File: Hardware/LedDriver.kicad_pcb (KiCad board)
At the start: 2 copper layers, 38 x 17 mm, 10 parts, among them J1 Led connector, U1 AP3019A

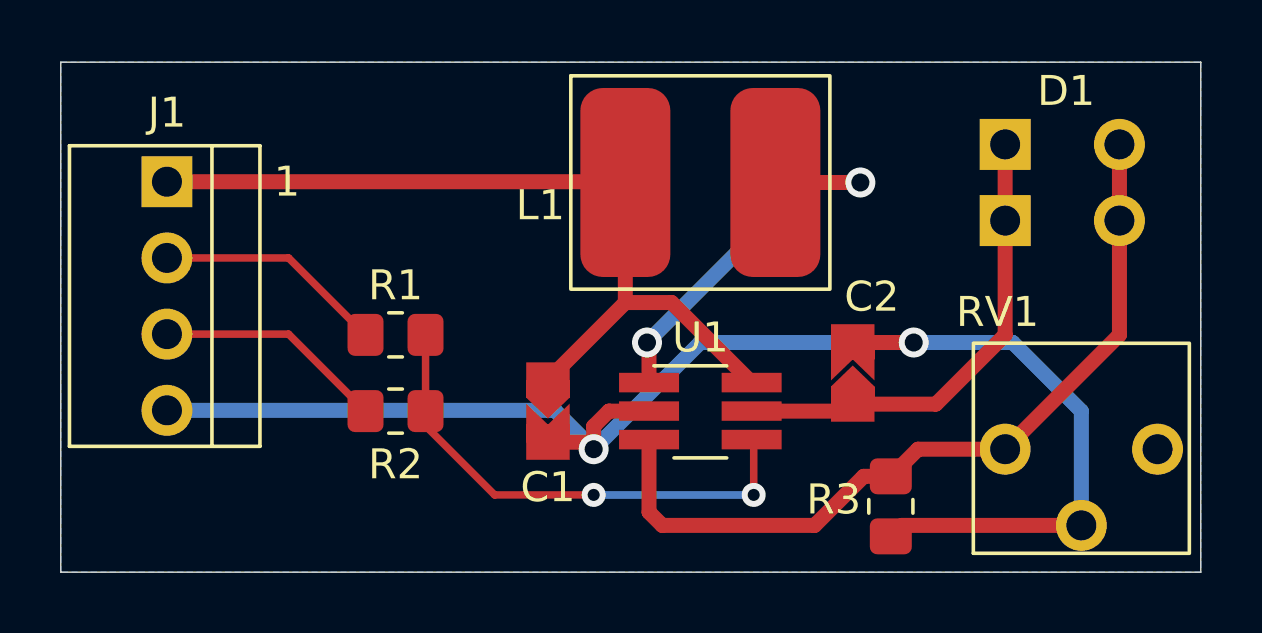
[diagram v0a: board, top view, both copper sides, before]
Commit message: ledDriver: added ground plane on top
+ added vias
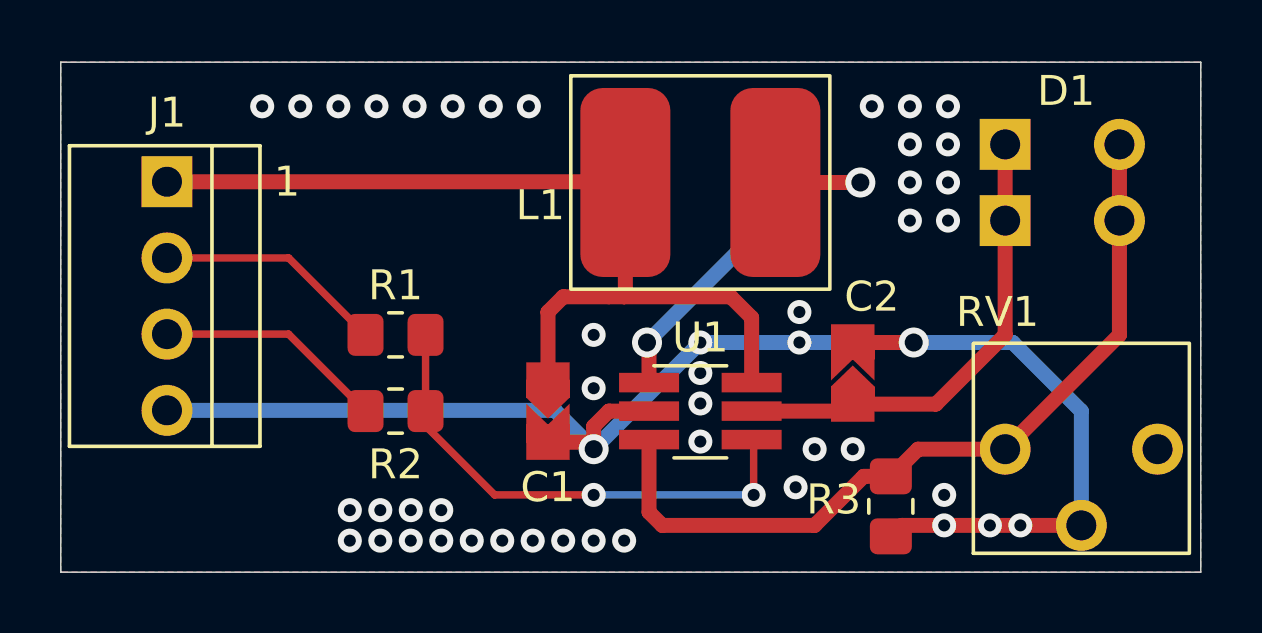
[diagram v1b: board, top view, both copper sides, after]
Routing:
- net VCC: track 28.3 -> 30.8 mm
- net GND: vias 2 -> 48
- added copper zone on F.Cu, net GND
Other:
- board text added: "Led driver Esseiva Nicolas 2023.05.07 - R01"
- board text removed: "Led driver Esseiva Nicolas 2023.04.07 - R00"
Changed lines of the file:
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@@
   )
   (gr_rect (start 126 76) (end 164 93) (layer "Edge.Cuts") (width 0.05) (fill none))
-  (gr_text "Led driver\nEsseiva Nicolas\n2023.04.07 - R00" (at 145 81.5) (layer "B.SilkS")
+  (gr_text "Led driver\nEsseiva Nicolas\n2023.05.07 - R01" (at 145 81.5) (layer "B.SilkS")
     (effects (font (size 1.5 1.5) (thickness 0.3)))
   )
@@
   (segment (start 129.54 79.985) (end 144.795 79.985) (width 0.5) (layer "F.Cu") (net 1))
   (segment (start 144.795 79.985) (end 144.82 80.01) (width 0.5) (layer "F.Cu") (net 1))
-  (segment (start 149.03 86.68) (end 146.3625 84.0125) (width 0.5) (layer "F.Cu") (net 1))
-  (segment (start 144.82 80.01) (end 144.82 84.0125) (width 0.5) (layer "F.Cu") (net 1))
-  (segment (start 144.82 84.0125) (end 142.24 86.5925) (width 0.5) (layer "F.Cu") (net 1))
-  (segment (start 146.3625 84.0125) (end 144.82 84.0125) (width 0.5) (layer "F.Cu") (net 1))
-  (segment (start 154.035 91.44) (end 160.02 91.44) (width 0.5) (layer "F.Cu") (net 2))
+  (segment (start 142.748 83.82) (end 142.24 84.328) (width 0.5) (layer "F.Cu") (net 1))
+  (segment (start 149.03 86.68) (end 149.03 84.514) (width 0.5) (layer "F.Cu") (net 1))
+  (segment (start 144.272 83.82) (end 142.748 83.82) (width 0.5) (layer "F.Cu") (net 1))
+  (segment (start 149.03 84.514) (end 148.336 83.82) (width 0.5) (layer "F.Cu") (net 1))
+  (segment (start 142.24 84.328) (end 142.24 86.5925) (width 0.5) (layer "F.Cu") (net 1))
+  (segment (start 148.336 83.82) (end 144.78 83.82) (width 0.5) (layer "F.Cu") (net 1))
+  (segment (start 144.82 80.01) (end 144.82 83.78) (width 0.5) (layer "F.Cu") (net 1))
+  (segment (start 144.82 83.78) (end 144.78 83.82) (width 0.5) (layer "F.Cu") (net 1))
+  (segment (start 144.78 83.82) (end 144.272 83.82) (width 0.5) (layer "F.Cu") (net 1))
+  (segment (start 157.988 91.44) (end 160.02 91.44) (width 0.5) (layer "F.Cu") (net 2))
+  (segment (start 154.035 91.44) (end 155.448 91.44) (width 0.5) (layer "F.Cu") (net 2))
+  (segment (start 156.972 91.44) (end 157.988 91.44) (width 0.5) (layer "F.Cu") (net 2))
   (segment (start 152.4215 85.344) (end 152.4 85.3225) (width 0.5) (layer "F.Cu") (net 2))
   (segment (start 145.61 87.63) (end 144.272 87.63) (width 0.5) (layer "F.Cu") (net 2))
   (segment (start 154.432 85.344) (end 152.4215 85.344) (width 0.5) (layer "F.Cu") (net 2))
   (segment (start 142.24 88.6675) (end 143.5315 88.6675) (width 0.5) (layer "F.Cu") (net 2))
+  (segment (start 155.448 91.44) (end 156.972 91.44) (width 0.5) (layer "F.Cu") (net 2))
   (segment (start 143.5315 88.6675) (end 143.764 88.9) (width 0.5) (layer "F.Cu") (net 2))
   (segment (start 153.67 91.805) (end 154.035 91.44) (width 0.5) (layer "F.Cu") (net 2))
   (segment (start 144.272 87.63) (end 143.764 88.138) (width 0.5) (layer "F.Cu") (net 2))
   (segment (start 143.764 88.138) (end 143.764 88.9) (width 0.5) (layer "F.Cu") (net 2))
+  (via (at 136.525 77.47) (size 0.8) (drill 0.4) (layers "F.Cu" "B.Cu") (free) (net 2))
+  (via (at 141.732 91.948) (size 0.8) (drill 0.4) (layers "F.Cu" "B.Cu") (free) (net 2))
+  (via (at 156.972 91.44) (size 0.8) (drill 0.4) (layers "F.Cu" "B.Cu") (net 2))
+  (via (at 139.065 77.47) (size 0.8) (drill 0.4) (layers "F.Cu" "B.Cu") (free) (net 2))
+  (via (at 154.305 77.47) (size 0.8) (drill 0.4) (layers "F.Cu" "B.Cu") (free) (net 2))
+  (via (at 143.764 91.948) (size 0.8) (drill 0.4) (layers "F.Cu" "B.Cu") (free) (net 2))
+  (via (at 157.988 91.44) (size 0.8) (drill 0.4) (layers "F.Cu" "B.Cu") (net 2))
+  (via (at 133.985 77.47) (size 0.8) (drill 0.4) (layers "F.Cu" "B.Cu") (free) (net 2))
+  (via (at 139.7 91.948) (size 0.8) (drill 0.4) (layers "F.Cu" "B.Cu") (free) (net 2))
+  (via (at 140.335 77.47) (size 0.8) (drill 0.4) (layers "F.Cu" "B.Cu") (free) (net 2))
+  (via (at 154.305 78.74) (size 0.8) (drill 0.4) (layers "F.Cu" "B.Cu") (free) (net 2))
+  (via (at 138.684 91.948) (size 0.8) (drill 0.4) (layers "F.Cu" "B.Cu") (free) (net 2))
+  (via (at 137.795 77.47) (size 0.8) (drill 0.4) (layers "F.Cu" "B.Cu") (free) (net 2))
+  (via (at 152.4 88.9) (size 0.8) (drill 0.4) (layers "F.Cu" "B.Cu") (free) (net 2))
+  (via (at 137.668 90.932) (size 0.8) (drill 0.4) (layers "F.Cu" "B.Cu") (free) (net 2))
+  (via (at 154.305 81.28) (size 0.8) (drill 0.4) (layers "F.Cu" "B.Cu") (free) (net 2))
   (via (at 143.764 88.9) (size 1) (drill 0.6) (layers "F.Cu" "B.Cu") (net 2))
+  (via (at 137.668 91.948) (size 0.8) (drill 0.4) (layers "F.Cu" "B.Cu") (free) (net 2))
+  (via (at 135.636 91.948) (size 0.8) (drill 0.4) (layers "F.Cu" "B.Cu") (free) (net 2))
+  (via (at 144.78 91.948) (size 0.8) (drill 0.4) (layers "F.Cu" "B.Cu") (free) (net 2))
+  (via (at 135.636 90.932) (size 0.8) (drill 0.4) (layers "F.Cu" "B.Cu") (free) (net 2))
+  (via (at 147.32 88.646) (size 0.8) (drill 0.4) (layers "F.Cu" "B.Cu") (free) (net 2))
+  (via (at 138.684 90.932) (size 0.8) (drill 0.4) (layers "F.Cu" "B.Cu") (free) (net 2))
+  (via (at 155.575 81.28) (size 0.8) (drill 0.4) (layers "F.Cu" "B.Cu") (free) (net 2))
+  (via (at 136.652 90.932) (size 0.8) (drill 0.4) (layers "F.Cu" "B.Cu") (free) (net 2))
+  (via (at 150.622 84.328) (size 0.8) (drill 0.4) (layers "F.Cu" "B.Cu") (free) (net 2))
+  (via (at 155.575 80.01) (size 0.8) (drill 0.4) (layers "F.Cu" "B.Cu") (free) (net 2))
+  (via (at 154.305 80.01) (size 0.8) (drill 0.4) (layers "F.Cu" "B.Cu") (free) (net 2))
+  (via (at 141.605 77.47) (size 0.8) (drill 0.4) (layers "F.Cu" "B.Cu") (free) (net 2))
+  (via (at 143.764 85.09) (size 0.8) (drill 0.4) (layers "F.Cu" "B.Cu") (free) (net 2))
+  (via (at 150.622 85.344) (size 0.8) (drill 0.4) (layers "F.Cu" "B.Cu") (net 2))
+  (via (at 150.495 90.17) (size 0.8) (drill 0.4) (layers "F.Cu" "B.Cu") (free) (net 2))
+  (via (at 155.448 91.44) (size 0.8) (drill 0.4) (layers "F.Cu" "B.Cu") (net 2))
+  (via (at 153.035 77.47) (size 0.8) (drill 0.4) (layers "F.Cu" "B.Cu") (free) (net 2))
+  (via (at 140.716 91.948) (size 0.8) (drill 0.4) (layers "F.Cu" "B.Cu") (free) (net 2))
+  (via (at 136.652 91.948) (size 0.8) (drill 0.4) (layers "F.Cu" "B.Cu") (free) (net 2))
+  (via (at 142.748 91.948) (size 0.8) (drill 0.4) (layers "F.Cu" "B.Cu") (free) (net 2))
+  (via (at 155.448 90.424) (size 0.8) (drill 0.4) (layers "F.Cu" "B.Cu") (free) (net 2))
+  (via (at 132.715 77.47) (size 0.8) (drill 0.4) (layers "F.Cu" "B.Cu") (free) (net 2))
+  (via (at 155.575 78.74) (size 0.8) (drill 0.4) (layers "F.Cu" "B.Cu") (free) (net 2))
+  (via (at 147.32 85.344) (size 0.8) (drill 0.4) (layers "F.Cu" "B.Cu") (net 2))
+  (via (at 155.575 77.47) (size 0.8) (drill 0.4) (layers "F.Cu" "B.Cu") (free) (net 2))
+  (via (at 147.32 86.36) (size 0.8) (drill 0.4) (layers "F.Cu" "B.Cu") (free) (net 2))
+  (via (at 135.255 77.47) (size 0.8) (drill 0.4) (layers "F.Cu" "B.Cu") (free) (net 2))
+  (via (at 151.13 88.9) (size 0.8) (drill 0.4) (layers "F.Cu" "B.Cu") (free) (net 2))
   (via (at 154.432 85.344) (size 1) (drill 0.6) (layers "F.Cu" "B.Cu") (net 2))
-  (segment (start 147.32 85.344) (end 154.432 85.344) (width 0.5) (layer "B.Cu") (net 2))
+  (via (at 143.764 86.868) (size 0.8) (drill 0.4) (layers "F.Cu" "B.Cu") (free) (net 2))
+  (via (at 147.32 87.376) (size 0.8) (drill 0.4) (layers "F.Cu" "B.Cu") (free) (net 2))
+  (segment (start 147.32 85.344) (end 150.622 85.344) (width 0.5) (layer "B.Cu") (net 2))
   (segment (start 157.734 85.344) (end 154.432 85.344) (width 0.5) (layer "B.Cu") (net 2))
+  (segment (start 150.622 85.344) (end 154.432 85.344) (width 0.5) (layer "B.Cu") (net 2))
   (segment (start 160.02 87.63) (end 157.734 85.344) (width 0.5) (layer "B.Cu") (net 2))
   (segment (start 142.469 87.605) (end 143.764 88.9) (width 0.5) (layer "B.Cu") (net 2))
@@
   (via (at 143.764 90.424) (size 0.8) (drill 0.4) (layers "F.Cu" "B.Cu") (net 8))
   (segment (start 143.764 90.424) (end 149.098 90.424) (width 0.25) (layer "B.Cu") (net 8))
-  (zone (net 2) (net_name "GND") (layer "B.Cu") (hatch edge 0.508)
+  (zone (net 2) (net_name "GND") (layers F&B.Cu) (hatch edge 0.508)
     (connect_pads (clearance 0.508))
     (min_thickness 0.254) (filled_areas_thickness no)
